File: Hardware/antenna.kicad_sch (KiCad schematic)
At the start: 16 parts, among them J13 J-0530471010, J17 252105, J18 252105, J20 252105, U13 HMC544AE, U14 SN74LVC1G14DCKR

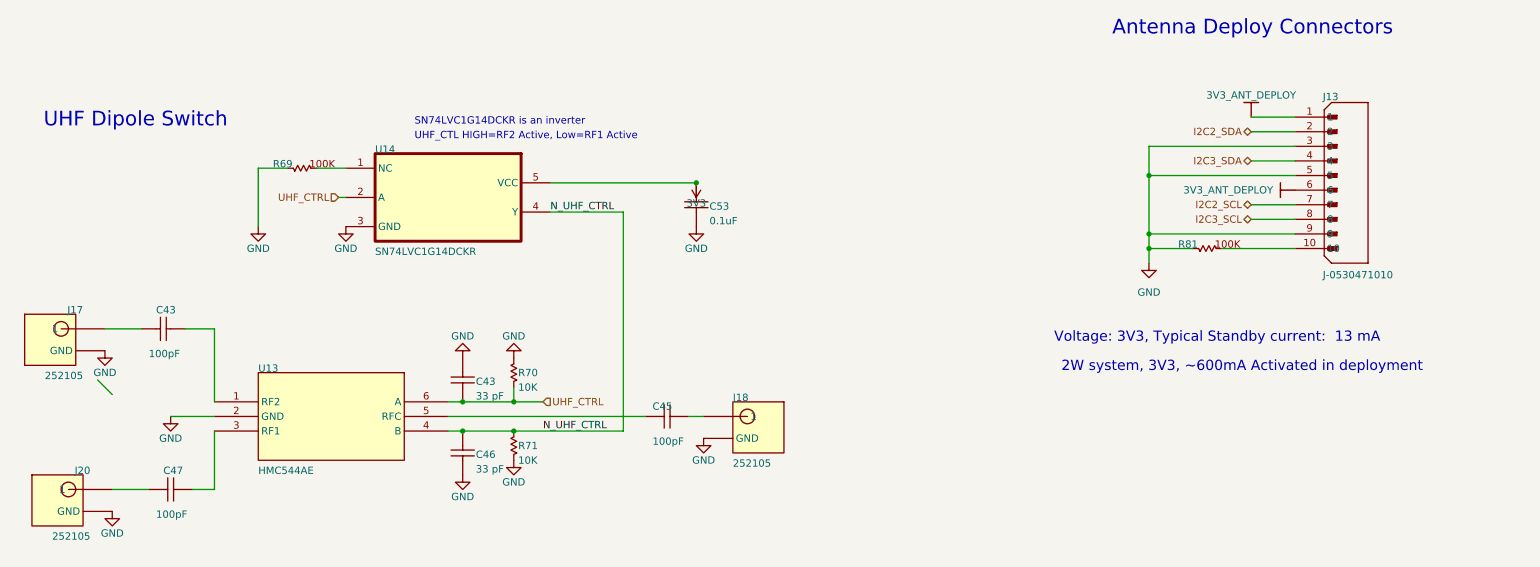
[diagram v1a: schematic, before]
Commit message: Add STM32 Reset Switch & RP2040 I2C pins
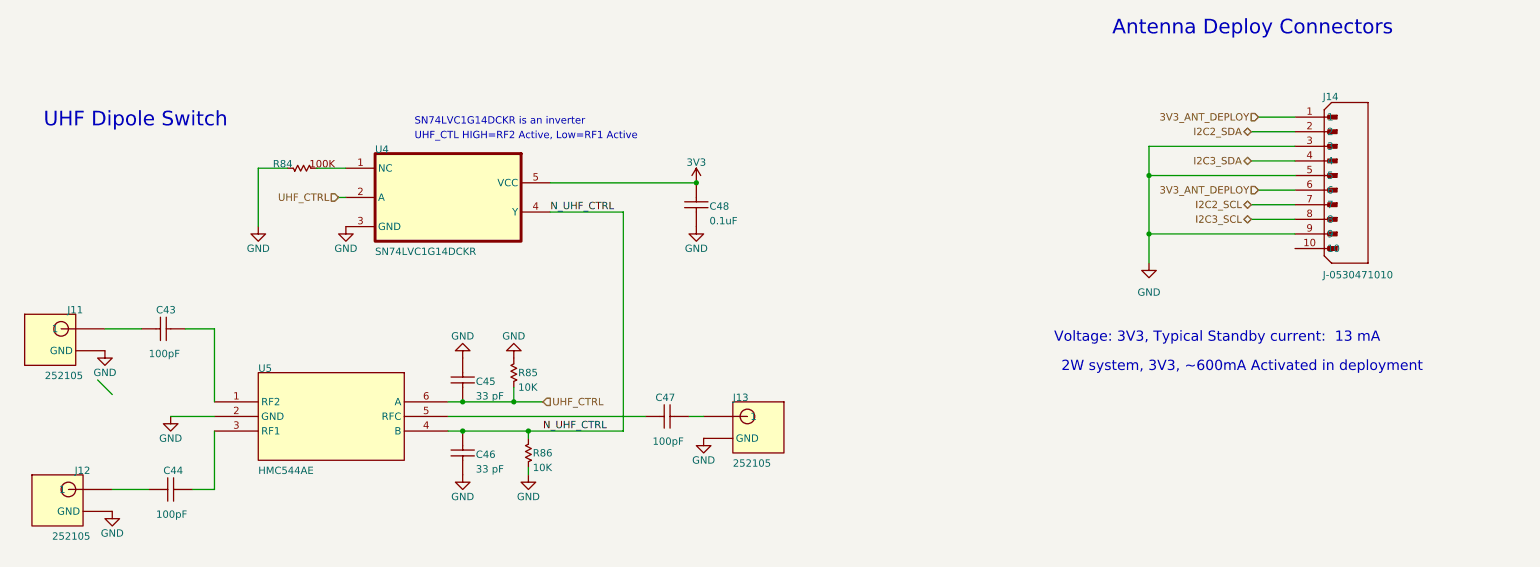
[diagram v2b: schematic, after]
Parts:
- removed R81: 100K, 0603, symbol OBC Development Board:root_0_RT-100K0-F-1/16W-0603_OBC Development Board.SchLib
- renumbered C47 to C44, C43 to C45, C45 to C47, C53 to C48, J17 to J11, J20 to J12, J18 to J13, J13 to J14, R69 to R84, R70 to R85, R71 to R86, U14 to U4, U13 to U5
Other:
- moved on the sheet: R86

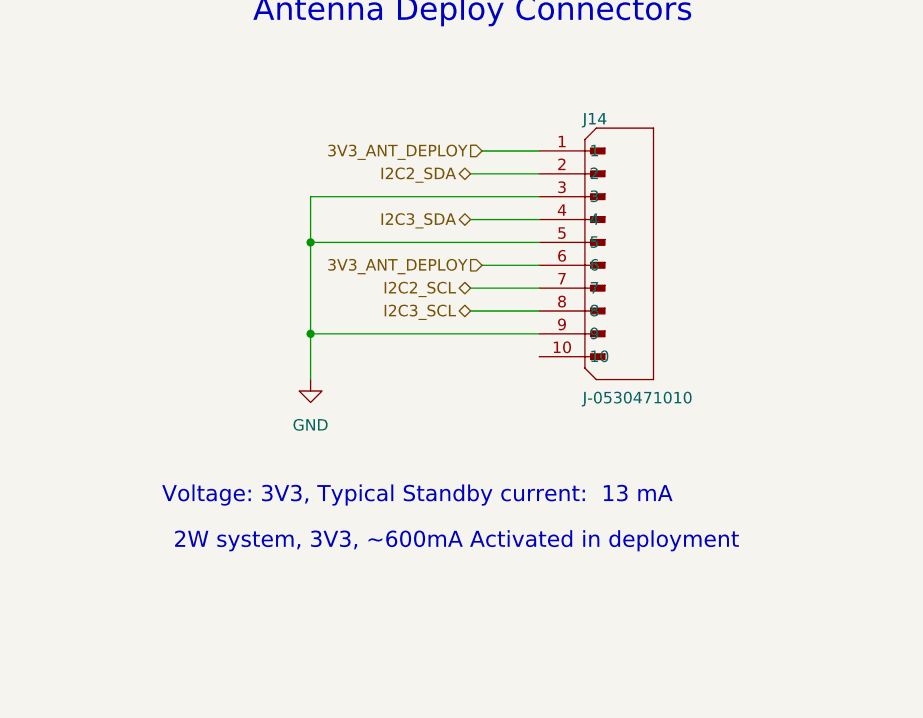
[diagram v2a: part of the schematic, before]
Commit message: Move ANT to RP2040
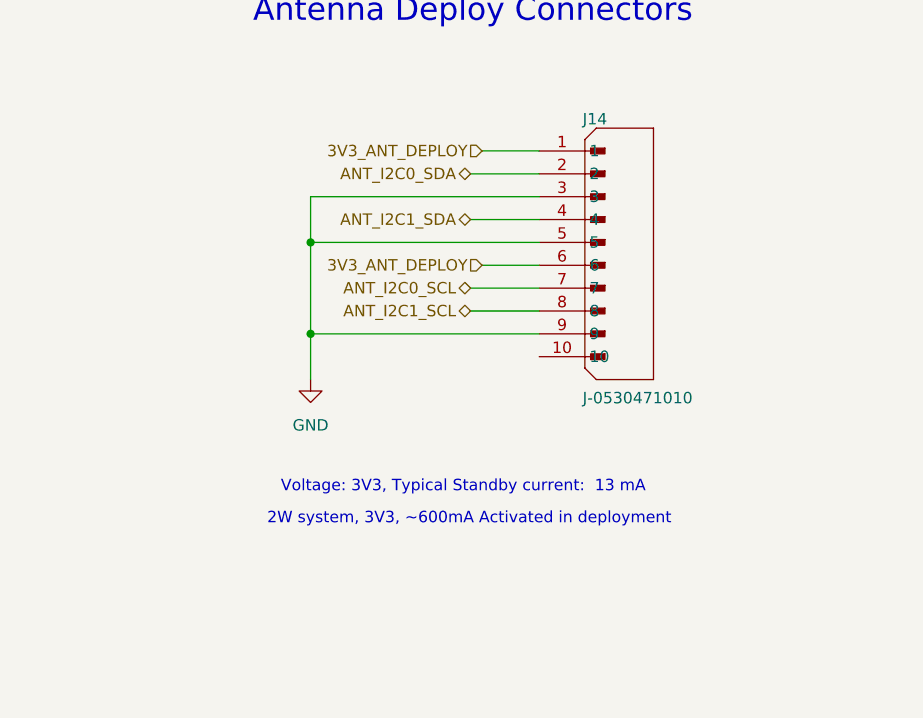
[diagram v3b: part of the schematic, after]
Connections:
- net I2C2_SCL renamed ANT_I2C0_SCL
- net I2C2_SDA renamed ANT_I2C0_SDA
- net I2C3_SCL renamed ANT_I2C1_SCL
- net I2C3_SDA renamed ANT_I2C1_SDA

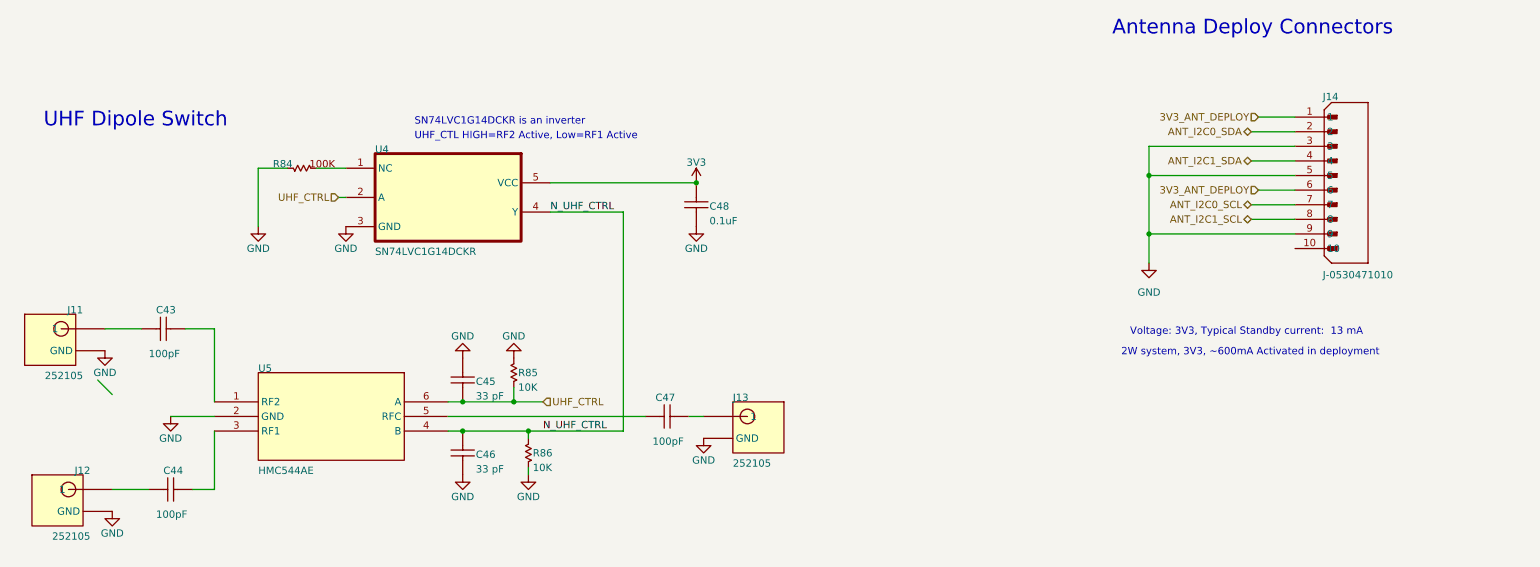
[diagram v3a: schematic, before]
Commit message: Add RP2040 SWD
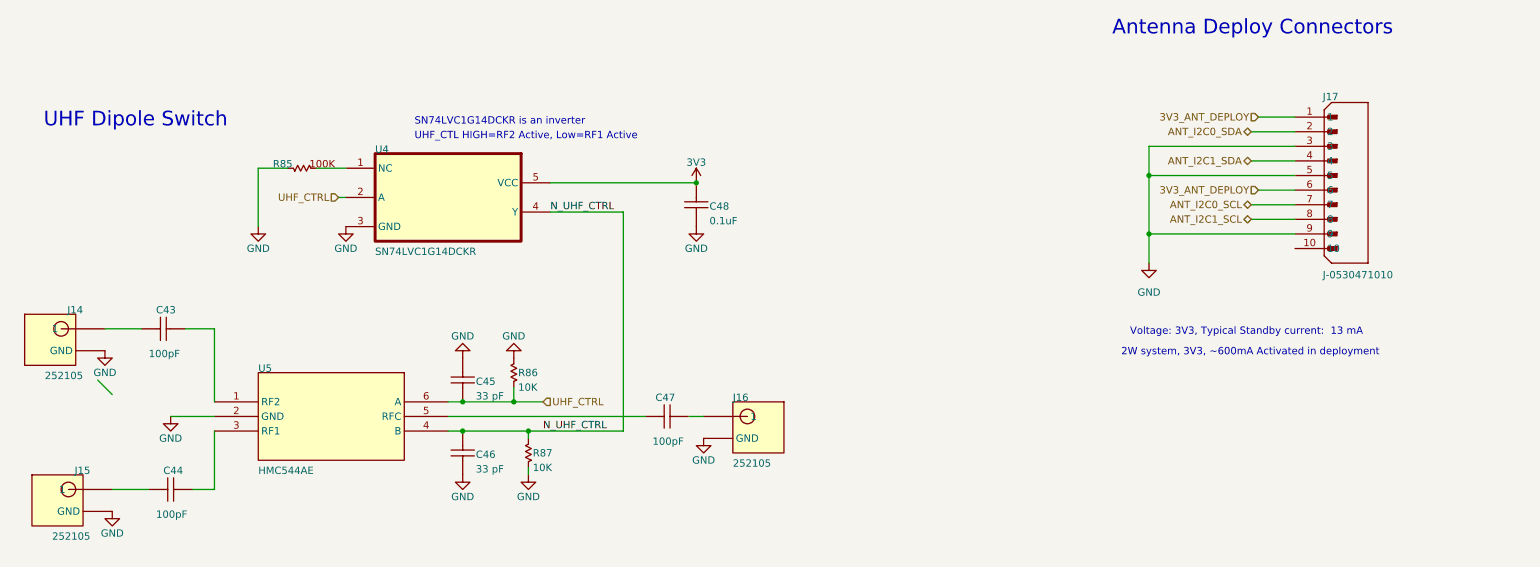
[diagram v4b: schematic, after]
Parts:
- renumbered J11 to J14, J12 to J15, J13 to J16, J14 to J17, R84 to R85, R85 to R86, R86 to R87
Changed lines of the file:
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@@
 		(on_board yes)
 		(dnp no)
-		(property "Reference" "J11"
+		(property "Reference" "J14"
 			(at 80.01 119.38 0)
 			(effects
@@
 			(project "CTS-SAT-2-OBC-PCB"
 				(path "/58243925-df8d-4fc1-899e-fce866d1d25a/368e4a7b-bdab-4813-9da8-67dfcdf79ec2"
-					(reference "J11")
+					(reference "J14")
 					(unit 1)
 				)
@@
 		(on_board yes)
 		(dnp no)
-		(property "Reference" "J13"
+		(property "Reference" "J16"
 			(at 193.04 134.62 0)
 			(effects
@@
 			(project "CTS-SAT-2-OBC-PCB"
 				(path "/58243925-df8d-4fc1-899e-fce866d1d25a/368e4a7b-bdab-4813-9da8-67dfcdf79ec2"
-					(reference "J13")
+					(reference "J16")
 					(unit 1)
 				)
@@
 		(on_board yes)
 		(dnp no)
-		(property "Reference" "R86"
+		(property "Reference" "R87"
 			(at 158.242 144.272 0)
 			(effects
@@
 			(project "CTS-SAT-2-OBC-PCB"
 				(path "/58243925-df8d-4fc1-899e-fce866d1d25a/368e4a7b-bdab-4813-9da8-67dfcdf79ec2"
-					(reference "R86")
+					(reference "R87")
 					(unit 1)
 				)
@@
 		(on_board yes)
 		(dnp no)
-		(property "Reference" "R85"
+		(property "Reference" "R86"
 			(at 155.702 130.302 0)
 			(effects
@@
 			(project "CTS-SAT-2-OBC-PCB"
 				(path "/58243925-df8d-4fc1-899e-fce866d1d25a/368e4a7b-bdab-4813-9da8-67dfcdf79ec2"
-					(reference "R85")
+					(reference "R86")
 					(unit 1)
 				)
@@
 		(on_board yes)
 		(dnp no)
-		(property "Reference" "#PWR0106"
+		(property "Reference" "#PWR0110"
 			(at 186.69 110.49 0)
 			(effects
@@
 			(project "CTS-SAT-2-OBC-PCB"
 				(path "/58243925-df8d-4fc1-899e-fce866d1d25a/368e4a7b-bdab-4813-9da8-67dfcdf79ec2"
-					(reference "#PWR0106")
+					(reference "#PWR0110")
 					(unit 1)
 				)
@@
 		(on_board yes)
 		(dnp no)
-		(property "Reference" "#PWR0107"
+		(property "Reference" "#PWR0111"
 			(at 187.96 147.32 0)
 			(effects
@@
 			(project "CTS-SAT-2-OBC-PCB"
 				(path "/58243925-df8d-4fc1-899e-fce866d1d25a/368e4a7b-bdab-4813-9da8-67dfcdf79ec2"
-					(reference "#PWR0107")
+					(reference "#PWR0111")
 					(unit 1)
 				)
@@
 		(on_board yes)
 		(dnp no)
-		(property "Reference" "J14"
+		(property "Reference" "J17"
 			(at 295.656 82.296 0)
 			(effects
@@
 			(project "CTS-SAT-2-OBC-PCB"
 				(path "/58243925-df8d-4fc1-899e-fce866d1d25a/368e4a7b-bdab-4813-9da8-67dfcdf79ec2"
-					(reference "J14")
+					(reference "J17")
 					(unit 1)
 				)
@@
 		(on_board yes)
 		(dnp no)
-		(property "Reference" "#PWR098"
+		(property "Reference" "#PWR0102"
 			(at 95.25 143.51 0)
 			(effects
@@
 			(project "CTS-SAT-2-OBC-PCB"
 				(path "/58243925-df8d-4fc1-899e-fce866d1d25a/368e4a7b-bdab-4813-9da8-67dfcdf79ec2"
-					(reference "#PWR098")
+					(reference "#PWR0102")
 					(unit 1)
 				)
@@
 		(on_board yes)
 		(dnp no)
-		(property "Reference" "#PWR017"
+		(property "Reference" "#PWR0101"
 			(at 85.09 160.02 0)
 			(effects
@@
 			(project "CTS-SAT-2-OBC-PCB"
 				(path "/58243925-df8d-4fc1-899e-fce866d1d25a/368e4a7b-bdab-4813-9da8-67dfcdf79ec2"
-					(reference "#PWR017")
+					(reference "#PWR0101")
 					(unit 1)
 				)
@@
 		(on_board yes)
 		(dnp no)
-		(property "Reference" "#PWR099"
+		(property "Reference" "#PWR0103"
 			(at 110.49 110.49 0)
 			(effects
@@
 			(project "CTS-SAT-2-OBC-PCB"
 				(path "/58243925-df8d-4fc1-899e-fce866d1d25a/368e4a7b-bdab-4813-9da8-67dfcdf79ec2"
-					(reference "#PWR099")
+					(reference "#PWR0103")
 					(unit 1)
 				)
@@
 		(on_board yes)
 		(dnp no)
-		(property "Reference" "#PWR0104"
+		(property "Reference" "#PWR0108"
 			(at 157.48 153.67 0)
 			(effects
@@
 			(project "CTS-SAT-2-OBC-PCB"
 				(path "/58243925-df8d-4fc1-899e-fce866d1d25a/368e4a7b-bdab-4813-9da8-67dfcdf79ec2"
-					(reference "#PWR0104")
+					(reference "#PWR0108")
 					(unit 1)
 				)
@@
 		(on_board yes)
 		(dnp no)
-		(property "Reference" "R84"
+		(property "Reference" "R85"
 			(at 113.03 93.98 0)
 			(effects
@@
 			(project "CTS-SAT-2-OBC-PCB"
 				(path "/58243925-df8d-4fc1-899e-fce866d1d25a/368e4a7b-bdab-4813-9da8-67dfcdf79ec2"
-					(reference "R84")
+					(reference "R85")
 					(unit 1)
 				)
@@
 		(on_board yes)
 		(dnp no)
-		(property "Reference" "#PWR0105"
+		(property "Reference" "#PWR0109"
 			(at 186.69 100.33 0)
 			(effects
@@
 			(project "CTS-SAT-2-OBC-PCB"
 				(path "/58243925-df8d-4fc1-899e-fce866d1d25a/368e4a7b-bdab-4813-9da8-67dfcdf79ec2"
-					(reference "#PWR0105")
+					(reference "#PWR0109")
 					(unit 1)
 				)
@@
 		(on_board yes)
 		(dnp no)
-		(property "Reference" "J12"
+		(property "Reference" "J15"
 			(at 81.28 147.32 0)
 			(effects
@@
 			(project "CTS-SAT-2-OBC-PCB"
 				(path "/58243925-df8d-4fc1-899e-fce866d1d25a/368e4a7b-bdab-4813-9da8-67dfcdf79ec2"
-					(reference "J12")
+					(reference "J15")
 					(unit 1)
 				)
@@
 		(dnp no)
 		(fields_autoplaced yes)
-		(property "Reference" "#PWR0108"
+		(property "Reference" "#PWR0112"
 			(at 265.43 116.84 0)
 			(effects
@@
 			(project "CTS-SAT-2-OBC-PCB"
 				(path "/58243925-df8d-4fc1-899e-fce866d1d25a/368e4a7b-bdab-4813-9da8-67dfcdf79ec2"
-					(reference "#PWR0108")
+					(reference "#PWR0112")
 					(unit 1)
 				)
@@
 		(on_board yes)
 		(dnp no)
-		(property "Reference" "#PWR015"
+		(property "Reference" "#PWR0100"
 			(at 83.82 132.08 0)
 			(effects
@@
 			(project "CTS-SAT-2-OBC-PCB"
 				(path "/58243925-df8d-4fc1-899e-fce866d1d25a/368e4a7b-bdab-4813-9da8-67dfcdf79ec2"
-					(reference "#PWR015")
+					(reference "#PWR0100")
 					(unit 1)
 				)
@@
 		(on_board yes)
 		(dnp no)
-		(property "Reference" "#PWR0103"
+		(property "Reference" "#PWR0107"
 			(at 154.94 120.65 0)
 			(effects
@@
 			(project "CTS-SAT-2-OBC-PCB"
 				(path "/58243925-df8d-4fc1-899e-fce866d1d25a/368e4a7b-bdab-4813-9da8-67dfcdf79ec2"
-					(reference "#PWR0103")
+					(reference "#PWR0107")
 					(unit 1)
 				)
@@
 		(on_board yes)
 		(dnp no)
-		(property "Reference" "#PWR0101"
+		(property "Reference" "#PWR0105"
 			(at 146.05 120.65 0)
 			(effects
@@
 			(project "CTS-SAT-2-OBC-PCB"
 				(path "/58243925-df8d-4fc1-899e-fce866d1d25a/368e4a7b-bdab-4813-9da8-67dfcdf79ec2"
-					(reference "#PWR0101")
+					(reference "#PWR0105")
 					(unit 1)
 				)
@@
 		(on_board yes)
 		(dnp no)
-		(property "Reference" "#PWR0100"
+		(property "Reference" "#PWR0104"
 			(at 125.73 110.49 0)
 			(effects
@@
 			(project "CTS-SAT-2-OBC-PCB"
 				(path "/58243925-df8d-4fc1-899e-fce866d1d25a/368e4a7b-bdab-4813-9da8-67dfcdf79ec2"
-					(reference "#PWR0100")
+					(reference "#PWR0104")
 					(unit 1)
 				)
@@
 		(on_board yes)
 		(dnp no)
-		(property "Reference" "#PWR0102"
+		(property "Reference" "#PWR0106"
 			(at 146.05 153.67 0)
 			(effects
@@
 			(project "CTS-SAT-2-OBC-PCB"
 				(path "/58243925-df8d-4fc1-899e-fce866d1d25a/368e4a7b-bdab-4813-9da8-67dfcdf79ec2"
-					(reference "#PWR0102")
+					(reference "#PWR0106")
 					(unit 1)
 				)
